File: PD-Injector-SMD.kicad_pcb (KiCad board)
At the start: 2 copper layers, 20 x 27 mm, 13 parts, among them P1 USB_C_Plug_USB2.0

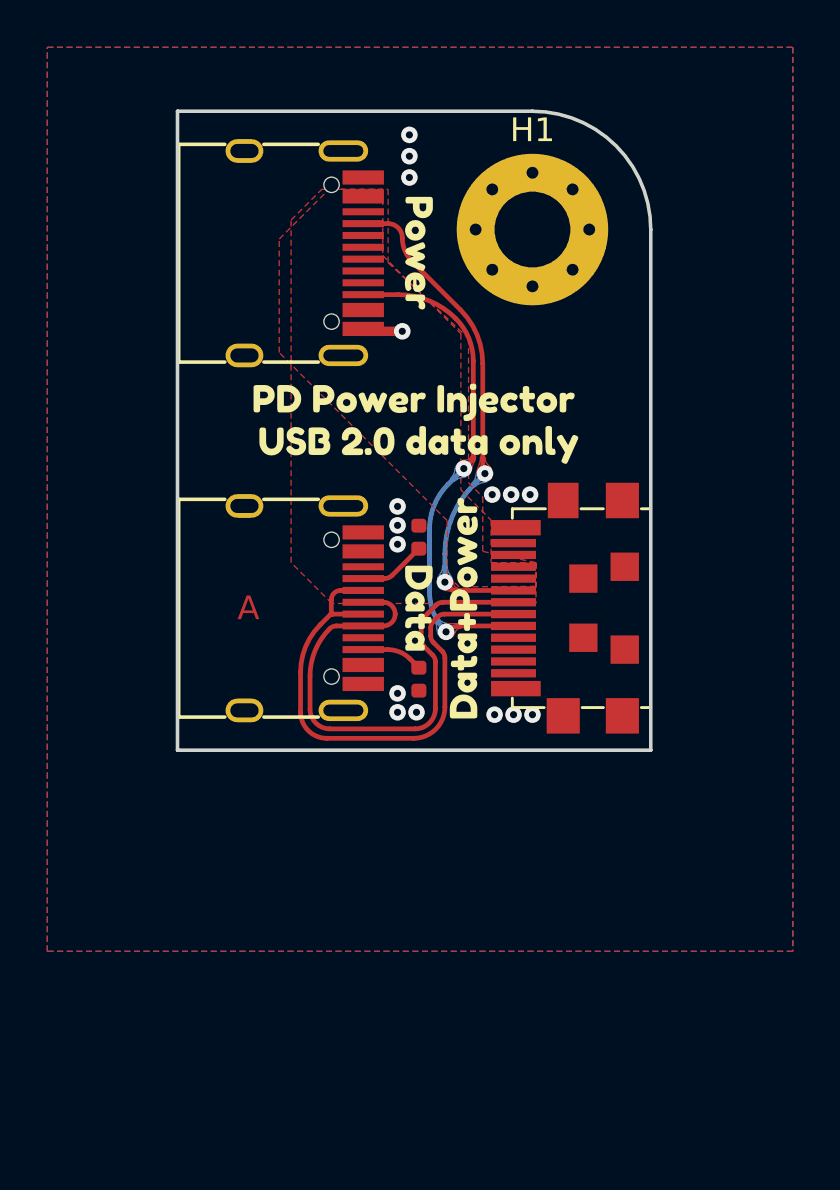
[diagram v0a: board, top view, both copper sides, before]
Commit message: change of form factor and further ECAD work
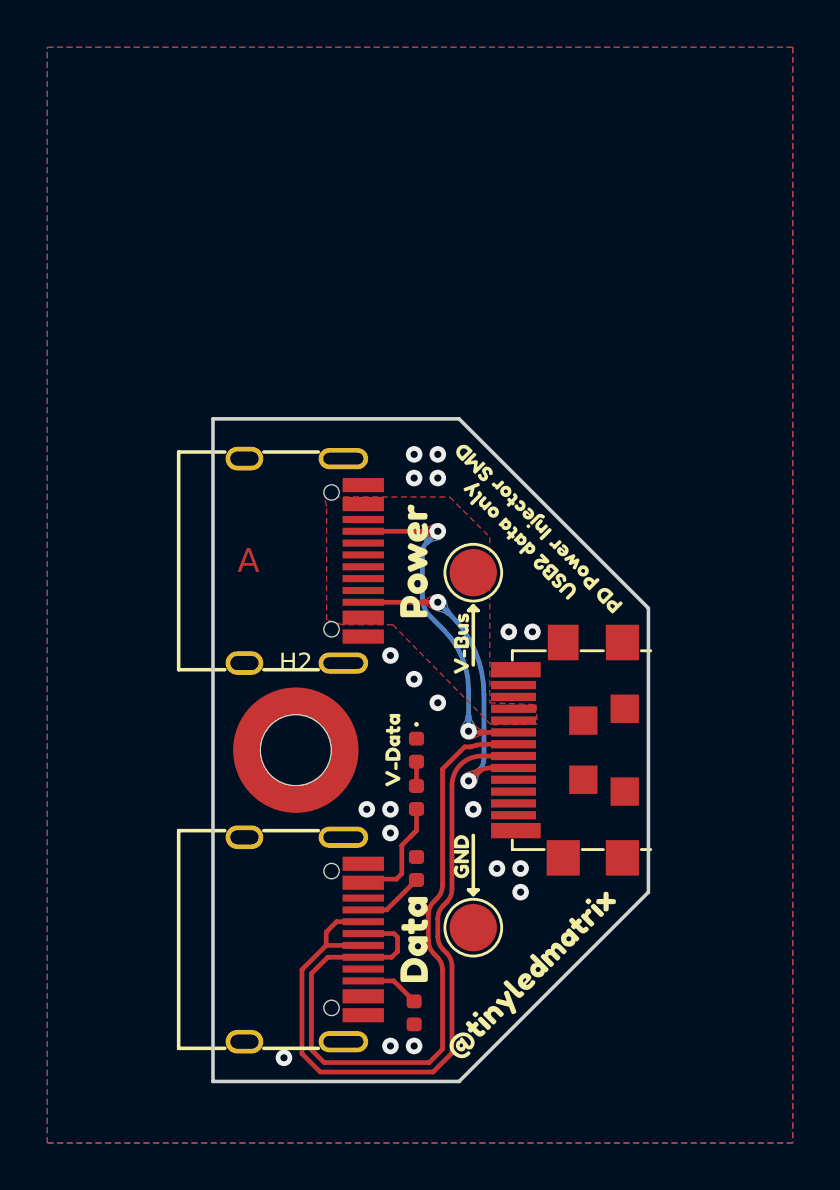
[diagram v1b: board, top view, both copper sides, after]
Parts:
- removed H1: MountingHole, MountingHole:MountingHole_3.2mm_M3_Pad_Via
- removed kibuzzard-63322182: G***, kibuzzard-63322182
- removed kibuzzard-633221BC: G***, kibuzzard-633221BC
- removed kibuzzard-633221E2: G***, kibuzzard-633221E2
- added D1: LED, LED_SMD:LED_0402_1005Metric, F.Cu at (165.1, 86.0)
- added H2: MountingHole, Eagle_WA-SMSI (rev21a):WA-SMSI_9774005243, F.Cu at (160.0, 86.0)
- added R3: 5.1k, Resistor_SMD:R_0402_1005Metric, F.Cu at (165.1, 88.0)
- added TP1: TestPoint, TestPoint:TestPoint_Pad_D2.0mm, F.Cu at (167.5, 78.5)
- added TP2: TestPoint, TestPoint:TestPoint_Pad_D2.0mm, F.Cu at (167.5, 93.5)
- added kibuzzard-63337211: G***, kibuzzard-63337211, F.Cu at (170.0, 95.5)
- added kibuzzard-63337259: G***, kibuzzard-63337259, B.Cu at (171.0, 86.0)
- added kibuzzard-6333729D: G***, kibuzzard-6333729D, B.Cu at (172.0, 86.0)
- added kibuzzard-633372BC: G***, kibuzzard-633372BC, B.Cu at (173.0, 86.0)
- added kibuzzard-633372D7: G***, kibuzzard-633372D7, B.Cu at (174.0, 86.0)
- added kibuzzard-6334B4B7: G***, kibuzzard-6334B4B7, F.Cu at (172.2, 78.6)
- added kibuzzard-6334B4C9: G***, kibuzzard-6334B4C9, F.Cu at (168.8, 75.0)
- added kibuzzard-6334B502: G***, kibuzzard-6334B502, F.Cu at (169.5, 77.1)
- added kibuzzard-6334B7AE: G***, kibuzzard-6334B7AE, F.Cu at (164.1, 86.0)
- added kibuzzard-6334B838: G***, kibuzzard-6334B838, F.Cu at (167.0, 81.5)
- added kibuzzard-6334B904: G***, kibuzzard-6334B904, F.Cu at (167.0, 90.5)
- moved kibuzzard-63336840 14.8 mm to (160.0, 94.0)
- moved R2 14.1 mm to (165.0, 97.1)
- moved kibuzzard-6333684F 14.1 mm to (160.0, 78.0)
- moved kibuzzard-63322175 14.0 mm to (165.0, 94.0), turned to 90 degrees
- moved R1 14.0 mm to (165.1, 91.0)
- moved USB-C2 14.0 mm to (159.7, 94.0)
- moved kibuzzard-63322190 13.0 mm to (165.0, 78.0), turned to 90 degrees
- moved USB-C1 13.0 mm to (159.7, 78.0)
- moved P1 6.00 mm to (169.4, 86.0)
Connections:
- USB-C2 pad A4: unconnected-(USB-C2-PadA4) -> Net-(USB-C2-PadA4)
- USB-C2 pad B9: unconnected-(USB-C2-PadA4) -> Net-(USB-C2-PadA4)
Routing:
- net /D+: track 22.6 -> 30.9 mm
- net /D-: track 22.8 -> 30.8 mm
- net /CC2P: track 21.3 -> 13.6 mm
- net /CC1P: track 21.3 -> 14.3 mm
- net Net-(USB-C2-PadA4): track 0.00 -> 4.93 mm
- net GND: track 1.67 -> 0.00 mm, vias 16 -> 19
- net Net-(D1-Pad2): track 0.00 -> 1.03 mm
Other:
- board size 20 x 27 mm -> 18.4 x 28 mm

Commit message: finalized PCB work for V0.1
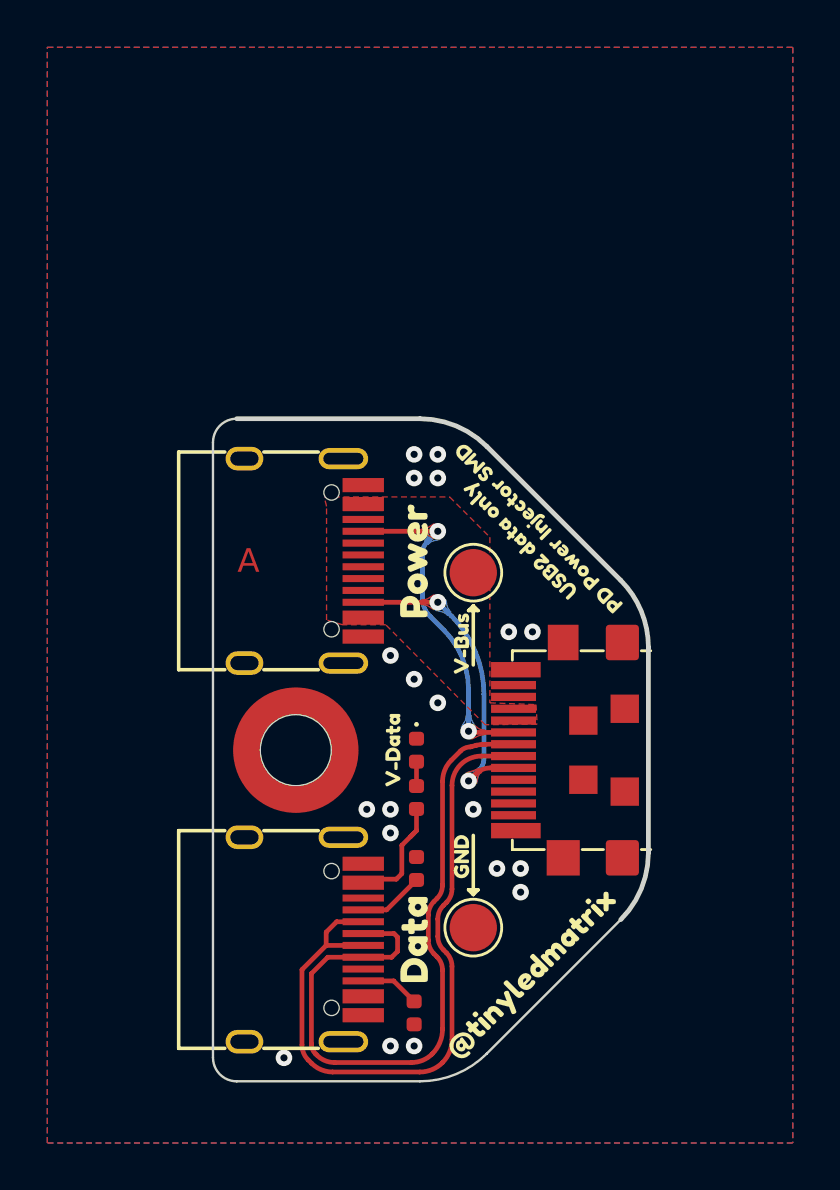
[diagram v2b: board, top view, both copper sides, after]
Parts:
- H2: value MountingHole -> M2x0.5mm SMD Spaccer
- turned kibuzzard-63337259 to -90 degrees
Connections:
- P1 pad A10: (no net) -> unconnected-(P1-PadA10)
- P1 pad A11: (no net) -> unconnected-(P1-PadA11)
- P1 pad B2: (no net) -> unconnected-(P1-PadB2)
- P1 pad B3: (no net) -> unconnected-(P1-PadB3)
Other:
- outline, holes or cut-outs redrawn
- rule pad_to_mask_clearance: 0.1 -> 0
